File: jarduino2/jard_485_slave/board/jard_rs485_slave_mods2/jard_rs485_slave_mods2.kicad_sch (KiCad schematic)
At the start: 0 parts

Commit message: Modification titre du schéma + Nomenclature
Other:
- note added: "Carte de commande d'un Oya Esclave RS485 (Avec Modules) Petite Carte"
- note removed: "Carte de commande d'un Oya Esclave RS485 (Avec ATMEGA328)"
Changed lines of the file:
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@@
     (comment 3 "1 sortie 12V/5A - 2 entrées TOR - 1 débimètre - 1 LED - Temp - RS485")
   )
-  (text "Carte de commande d'un Oya\nEsclave RS485 (Avec ATMEGA328)"
-    (at 39.37 62.23 0)
+  (text "Carte de commande d'un Oya\nEsclave RS485 (Avec Modules)\nPetite Carte"
+    (at 46.99 71.12 0)
     (effects (font (face "Arial") (size 10 10)) (justify left bottom))
   )
-  (sheet (at 92.71 95.25) (size 54.61 39.37) (fields_autoplaced)
+  (sheet (at 92.71 105.41) (size 54.61 39.37) (fields_autoplaced)
     (stroke (width 0.1524) (type solid))
     (fill (color 255 194 126 1.0000))
-    (property "Sheetname" "UC" (at 92.71 94.5384 0)
+    (property "Sheetname" "UC" (at 92.71 104.6984 0)
       (effects (font (size 1.27 1.27)) (justify left bottom))
     )
-    (property "Sheetfile" "uc.kicad_sch" (at 92.71 135.2046 0)
+    (property "Sheetfile" "uc.kicad_sch" (at 92.71 145.3646 0)
       (effects (font (size 1.27 1.27)) (justify left top))
     )
@@
     )
   )
-  (sheet (at 171.45 95.25) (size 41.91 38.1) (fields_autoplaced)
+  (sheet (at 171.45 105.41) (size 41.91 38.1) (fields_autoplaced)
     (stroke (width 0.1524) (type solid))
     (fill (color 153 145 255 1.0000))
-    (property "Sheetname" "ES" (at 171.45 94.5384 0)
+    (property "Sheetname" "ES" (at 171.45 104.6984 0)
       (effects (font (size 1.27 1.27)) (justify left bottom))
     )
-    (property "Sheetfile" "ES.kicad_sch" (at 171.45 133.9346 0)
+    (property "Sheetfile" "ES.kicad_sch" (at 171.45 144.0946 0)
       (effects (font (size 1.27 1.27)) (justify left top))
     )

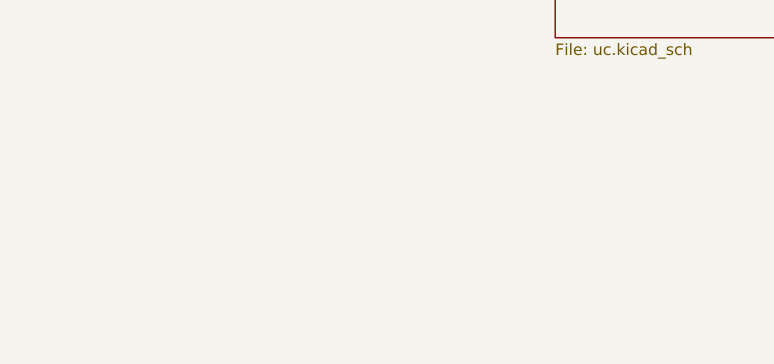
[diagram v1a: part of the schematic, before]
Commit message: Déplacement piste LED car trop proche du bord
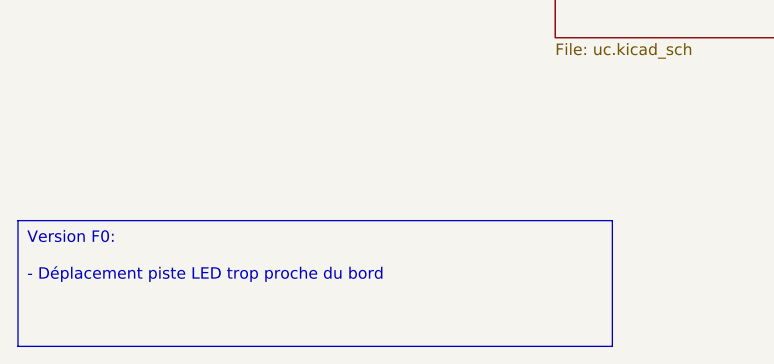
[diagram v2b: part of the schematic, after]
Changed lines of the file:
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@@
   (title_block
     (title "Carte de commande d'un OYA - Esclave RS485")
-    (date "2024-04-13")
-    (rev "E0")
+    (date "2024-04-27")
+    (rev "F0")
     (company "BPC")
     (comment 1 "Technologie avec modules Arduino / Petite carte")
@@
     (comment 3 "1 sortie 12V/5A - 2 entrées TOR - 1 débimètre - 1 LED - Temp - RS485")
   )
+  (text_box "Version F0:\n\n- Déplacement piste LED trop proche du bord"
+    (at 33.02 165.1 0) (size 66.04 13.97)
+    (stroke (width 0) (type default))
+    (fill (type none))
+    (effects (font (size 1.27 1.27)) (justify left top))
+  )
   (text "Carte de commande d'un Oya\nEsclave RS485 (Avec Modules)\nPetite Carte"

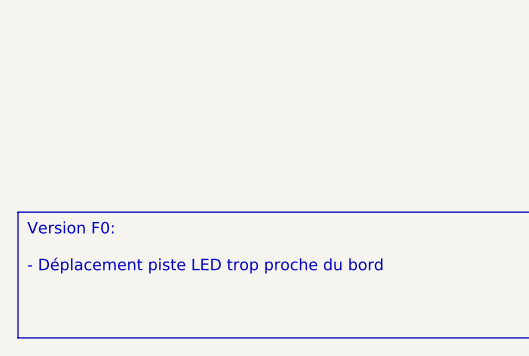
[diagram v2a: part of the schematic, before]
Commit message: Inversion RX/TX 485
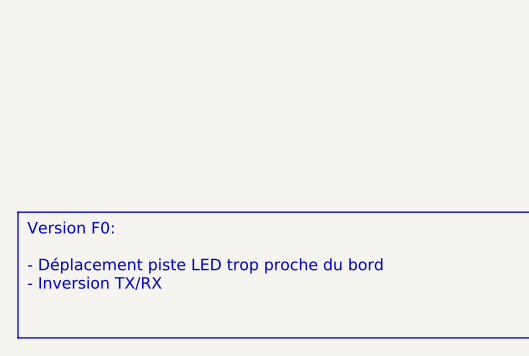
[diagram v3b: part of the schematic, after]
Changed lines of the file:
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@@
   (title_block
     (title "Carte de commande d'un OYA - Esclave RS485")
-    (date "2024-04-27")
+    (date "2024-05-04")
     (rev "F0")
     (company "BPC")
@@
     (comment 3 "1 sortie 12V/5A - 2 entrées TOR - 1 débimètre - 1 LED - Temp - RS485")
   )
-  (text_box "Version F0:\n\n- Déplacement piste LED trop proche du bord"
+  (text_box "Version F0:\n\n- Déplacement piste LED trop proche du bord\n- Inversion TX/RX"
     (at 33.02 165.1 0) (size 66.04 13.97)
     (stroke (width 0) (type default))

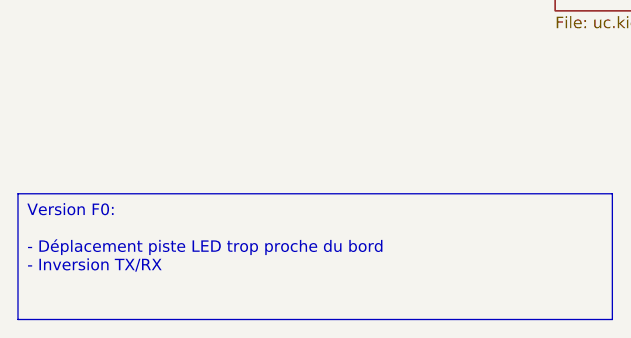
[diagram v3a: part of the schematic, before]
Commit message: Agrandissement pastilles Mod RS485
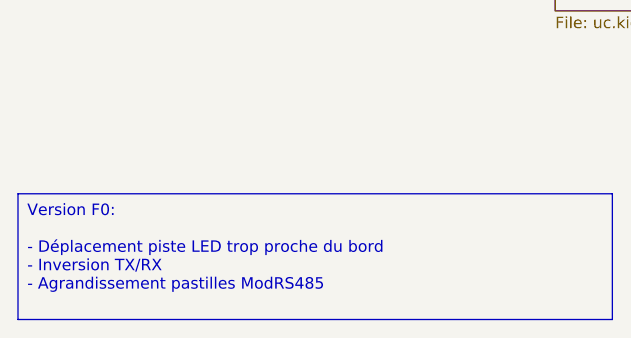
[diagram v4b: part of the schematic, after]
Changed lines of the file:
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@@
   (title_block
     (title "Carte de commande d'un OYA - Esclave RS485")
-    (date "2024-05-04")
+    (date "2024-05-17")
     (rev "F0")
     (company "BPC")
@@
     (comment 3 "1 sortie 12V/5A - 2 entrées TOR - 1 débimètre - 1 LED - Temp - RS485")
   )
-  (text_box "Version F0:\n\n- Déplacement piste LED trop proche du bord\n- Inversion TX/RX"
+  (text_box "Version F0:\n\n- Déplacement piste LED trop proche du bord\n- Inversion TX/RX\n- Agrandissement pastilles ModRS485"
     (at 33.02 165.1 0) (size 66.04 13.97)
     (stroke (width 0) (type default))
